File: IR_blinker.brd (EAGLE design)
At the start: 13.8 x 11.9 mm, 11 parts, among them IC1 PIC16F15214-E/SN, Q1 DMG2302UK

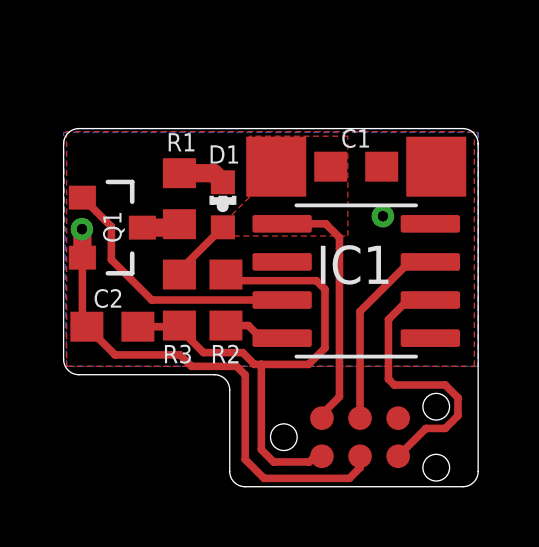
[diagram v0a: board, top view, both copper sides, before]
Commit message: Linear Regulator added. Passives added to MCLR.
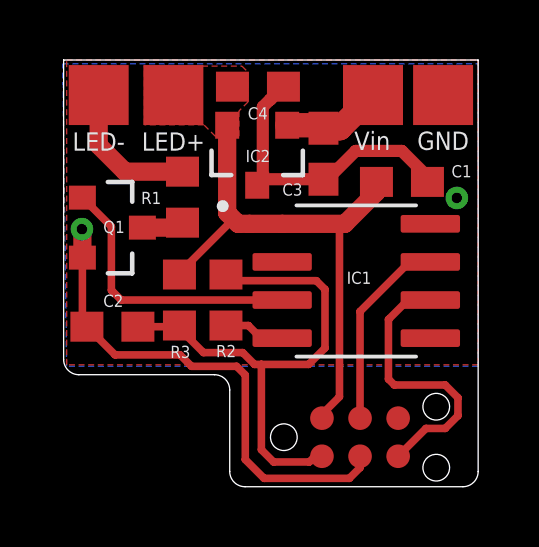
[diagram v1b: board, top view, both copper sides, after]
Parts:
- removed D1: APT1608F3C, led:CHIP-LED0603
- added C3: 10u, rcl:C0603
- added C4: 1u, rcl:C0603
- added IC2: AP7375-33SA, Diodes_Inc:SOT23
- added TP3, TP4: TPTP20SQ, testpad:TP20SQ
- moved TP1 4.01 mm to (10.5, 13.1)
- moved TP2 2.40 mm to (12.8, 13.1)
- moved C1 1.61 mm to (11.4, 10.2)
- moved R1 0.11 mm to (4.11, 9.65)
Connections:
- removed net +5V: C1.1, D1.A, IC1.1, J1.2, R3.2, TP1.TP
- removed net N$2: D1.C, R1.2
- new net LED_RETURN: R1.2, TP4.TP
- new net VDD: C1.1, C4.2, IC1.1, IC2.2, J1.2, R3.2, TP3.TP
- new net VIN: C3.2, IC2.1, TP1.TP
- net GND: now also C3.1, C4.1, IC2.3
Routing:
- net VDD: track 0.00 -> 18.7 mm
- net +5V: track 10.5 -> 0.00 mm
- net GND: track 16.7 -> 27.0 mm
- net LED_RETURN: track 0.00 -> 5.43 mm
- net VIN: track 0.00 -> 3.36 mm
- net N$2: track 1.57 -> 0.00 mm
- net N$3: track 8.72 -> 9.31 mm
- added copper zone on layer 1, net VDD
- removed copper zone on layer 1, net +5V
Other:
- board size 13.8 x 11.9 mm -> 13.8 x 14.2 mm
- board text added: "GND"
- board text added: "LED+"
- board text added: "LED-"
- board text added: "Vin"
